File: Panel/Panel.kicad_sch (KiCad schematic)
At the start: 72 parts, among them J1 Conn_01x03, J10 Conn_01x02, J11 Conn_01x03, J12 Conn_01x03, J2 USB_C_Receptacle_USB2.0, J3 Conn_01x02, J4 Conn_02x06_Odd_Even, J5 Conn_01x07, J6 Conn_01x02, J7 Conn_01x02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

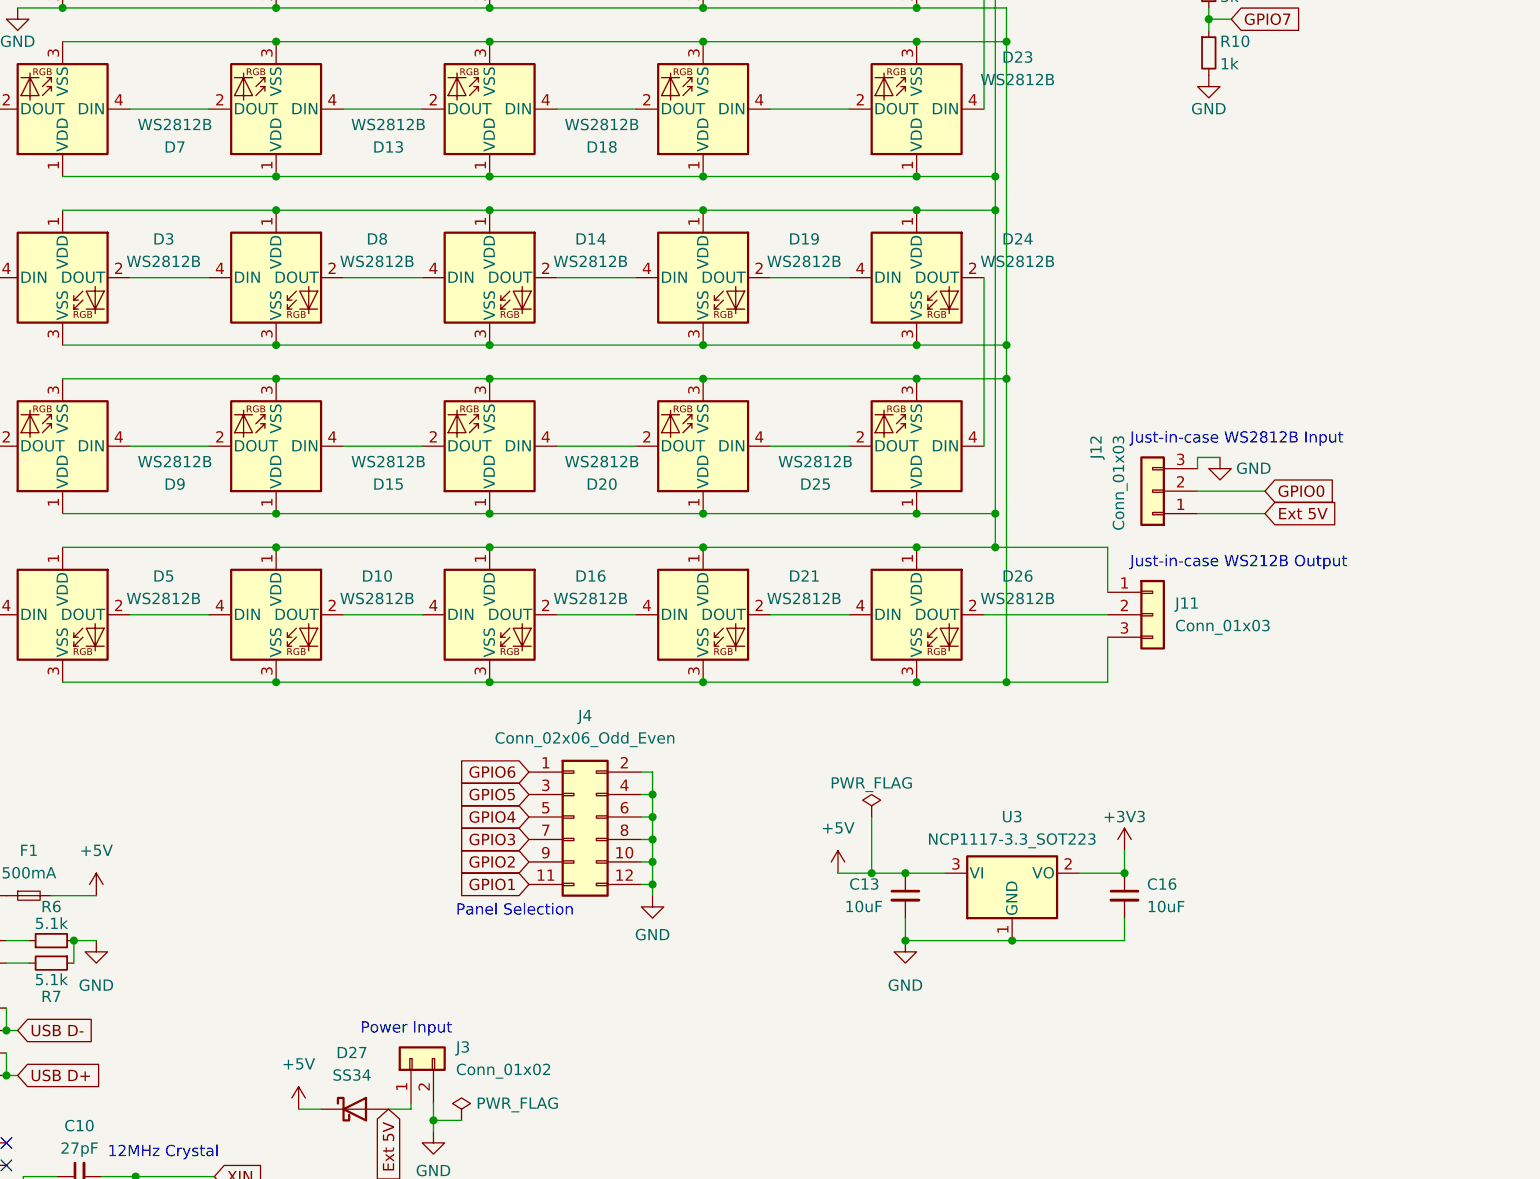
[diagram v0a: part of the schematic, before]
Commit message: Add RS485 functionality & addons, several fixes
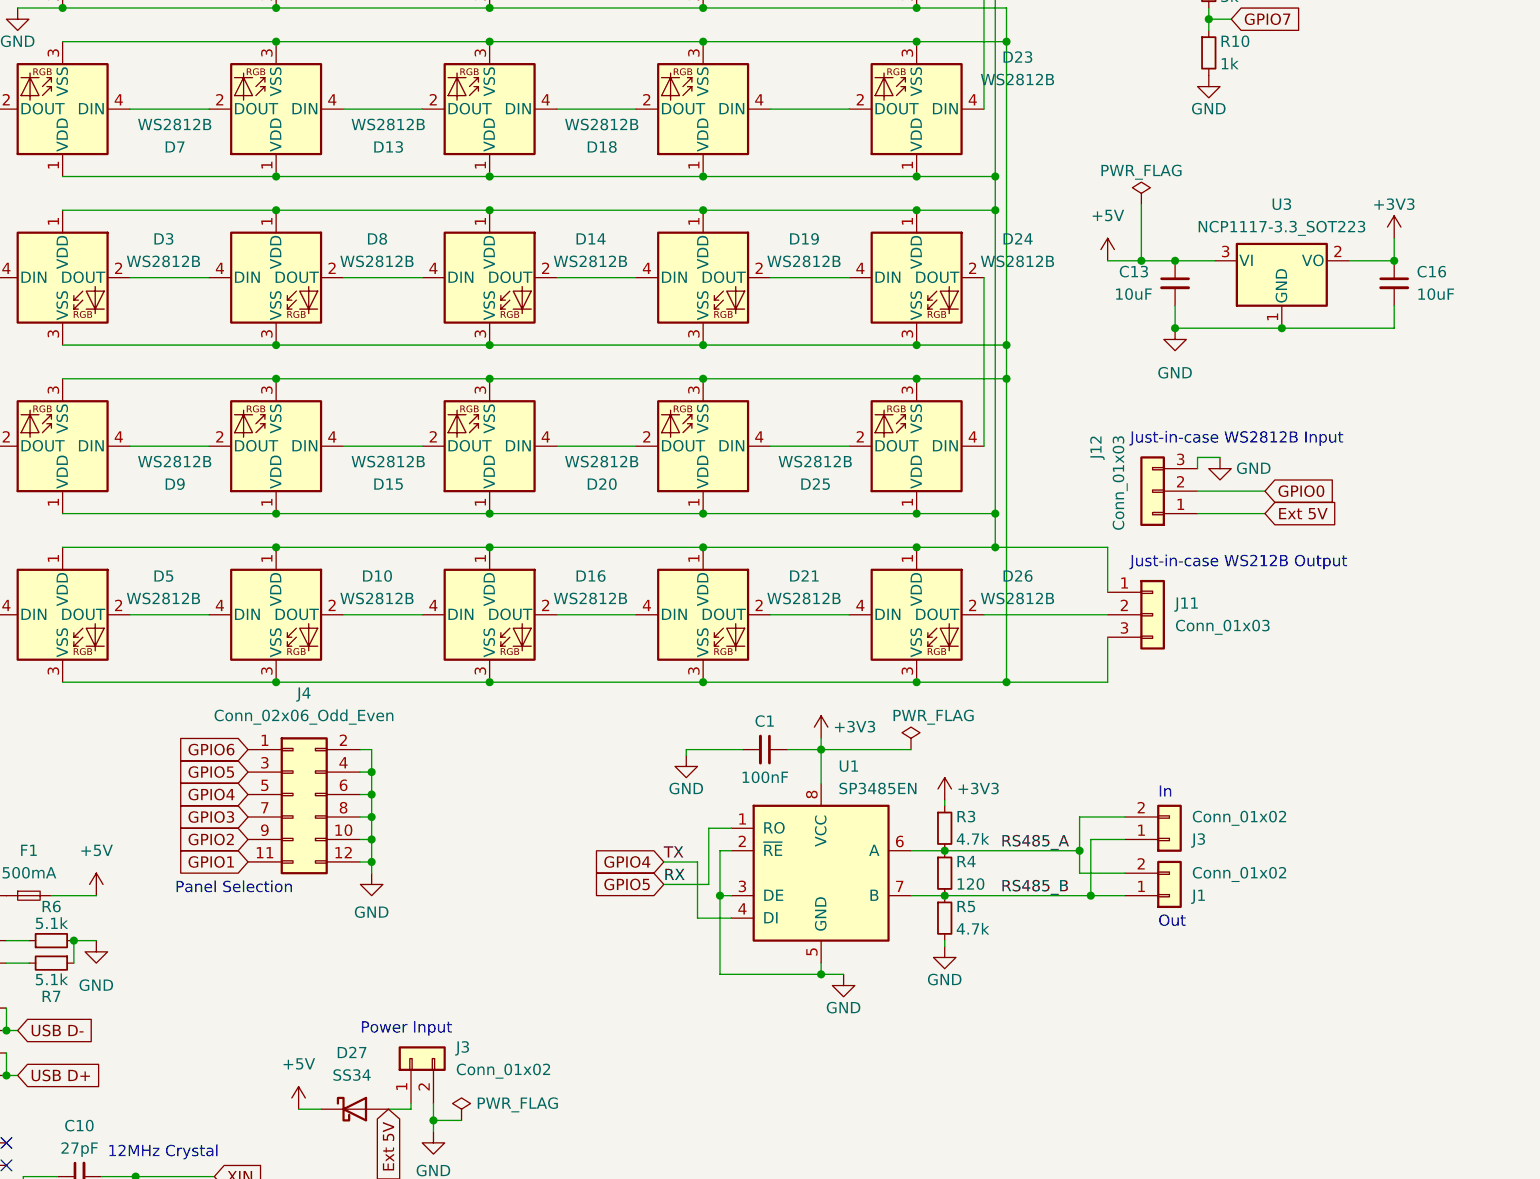
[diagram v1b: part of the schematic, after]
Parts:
- added C1: 100nF, Capacitor_SMD:C_0805_2012Metric_Pad1.18x1.45mm_HandSolder, symbol Device:C_Small
- added J1, J3: Conn_01x02, Connector_JST:JST_XH_S2B-XH-A_1x02_P2.50mm_Horizontal, symbol Connector_Generic:Conn_01x02
- added R3, R5: 4.7k, Resistor_SMD:R_0805_2012Metric_Pad1.20x1.40mm_HandSolder, symbol Device:R_Small
- added R4: 120, Resistor_SMD:R_0805_2012Metric_Pad1.20x1.40mm_HandSolder, symbol Device:R_Small
- added U1: SP3485EN, Package_SO:SOIC-8_3.9x4.9mm_P1.27mm, symbol Interface_UART:SP3485EN
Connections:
- net +3V3: now also C1.1, R3.1, U1.8 (VCC)
- net GND: now also C1.2, R5.2, U1.2 (~{RE}), U1.3 (DE), U1.5 (GND)
- net GPIO4: now also U1.4 (DI)
- net GPIO5: now also U1.1 (RO)
- new net RS485_A: J1.2 (Pin_2), J3.2 (Pin_2), R3.2, R4.1, U1.6 (A)
- new net RS485_B: J1.1 (Pin_1), J3.1 (Pin_1), R4.2, R5.1, U1.7 (B)
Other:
- note added: "In"
- note added: "Out"
- moved on the sheet: C13, C16, J4, U3

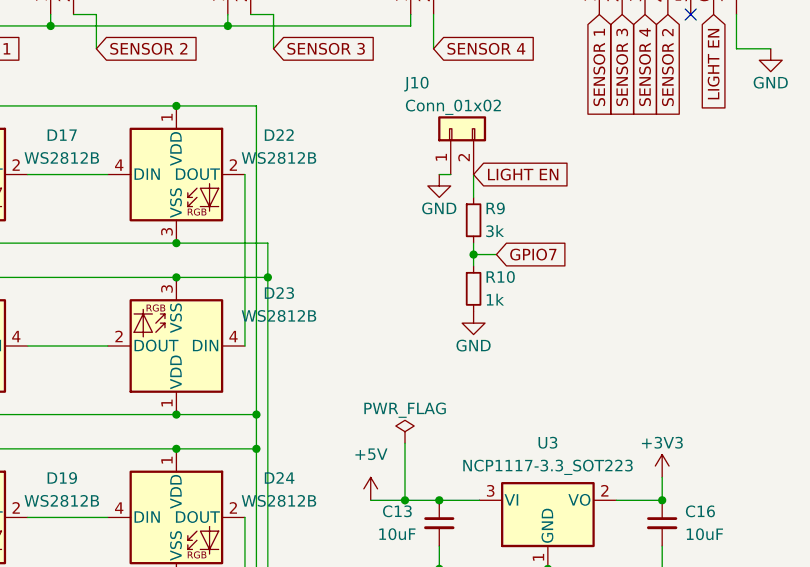
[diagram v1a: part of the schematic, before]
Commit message: Add voltage divider bypass for home pad use
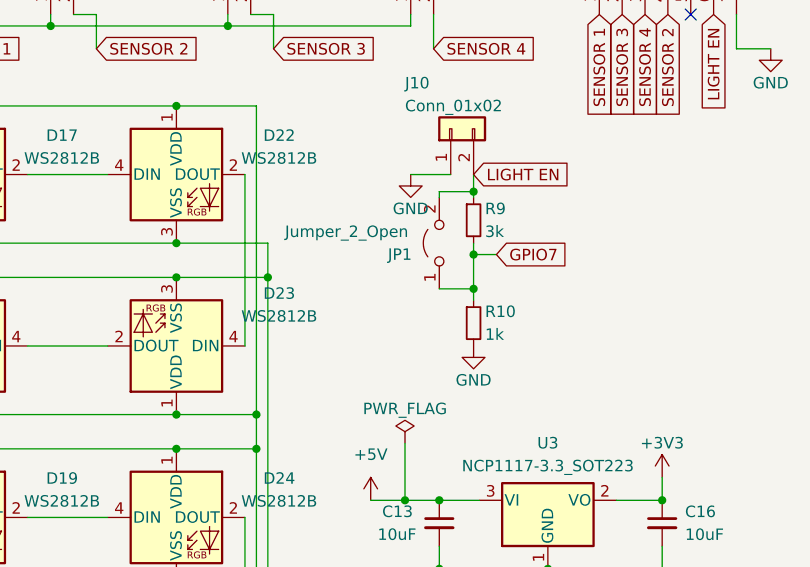
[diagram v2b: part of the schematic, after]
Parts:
- added JP1: Jumper_2_Open, Jumper:SolderJumper-2_P1.3mm_Open_RoundedPad1.0x1.5mm, symbol Jumper:Jumper_2_Open
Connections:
- net GPIO7: now also JP1.1 (A)
- net LIGHT EN: now also JP1.2 (B)
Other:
- moved on the sheet: R10
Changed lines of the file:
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@@
   (junction (at 113.03 171.45) (diameter 0) (color 0 0 0 0)
   )
+  (junction (at 248.92 55.88) (diameter 0) (color 0 0 0 0)
+  )
   (junction (at 191.77 88.9) (diameter 0) (color 0 0 0 0)
   )
   (junction (at 116.205 17.78) (diameter 0) (color 0 0 0 0)
   )
+  (junction (at 248.92 45.085) (diameter 0) (color 0 0 0 0)
+  )
   (junction (at 143.51 88.9) (diameter 0) (color 0 0 0 0)
   )
@@
     (stroke (width 0) (type default))
   )
-  (wire (pts (xy 245.11 43.18) (xy 246.38 43.18))
+  (wire (pts (xy 241.935 43.18) (xy 246.38 43.18))
     (stroke (width 0) (type default))
   )
@@
     (stroke (width 0) (type default))
   )
+  (wire (pts (xy 245.11 45.085) (xy 248.92 45.085))
+    (stroke (width 0) (type default))
+  )
   (wire (pts (xy 201.93 26.67) (xy 201.93 25.4))
     (stroke (width 0) (type default))
@@
     (stroke (width 0) (type default))
   )
+  (wire (pts (xy 248.92 55.88) (xy 248.92 57.15))
+    (stroke (width 0) (type default))
+  )
   (wire (pts (xy 24.765 158.75) (xy 27.305 158.75))
     (stroke (width 0) (type default))
@@
     (stroke (width 0) (type default))
   )
-  (wire (pts (xy 248.92 52.07) (xy 248.92 53.34))
+  (wire (pts (xy 248.92 52.07) (xy 248.92 55.88))
     (stroke (width 0) (type default))
   )
@@
     (stroke (width 0) (type default))
   )
-  (wire (pts (xy 248.92 43.18) (xy 248.92 45.72))
+  (wire (pts (xy 248.92 43.18) (xy 248.92 45.085))
     (stroke (width 0) (type default))
   )
@@
     (stroke (width 0) (type default))
   )
+  (wire (pts (xy 245.11 55.88) (xy 248.92 55.88))
+    (stroke (width 0) (type default))
+  )
   (wire (pts (xy 31.115 178.435) (xy 43.18 178.435))
     (stroke (width 0) (type default))
@@
     (stroke (width 0) (type default))
   )
+  (wire (pts (xy 245.11 45.72) (xy 245.11 45.085))
+    (stroke (width 0) (type default))
+  )
   (wire (pts (xy 95.885 39.37) (xy 95.885 38.1))
     (stroke (width 0) (type default))
@@
     (stroke (width 0) (type default))
   )
+  (wire (pts (xy 248.92 45.085) (xy 248.92 45.72))
+    (stroke (width 0) (type default))
+  )
   (wire (pts (xy 127 81.28) (xy 135.89 81.28))
     (stroke (width 0) (type default))
@@
     )
   )
-  (symbol (lib_id "power:GND") (at 245.11 43.18 0) (unit 1)
+  (symbol (lib_id "power:GND") (at 241.935 43.18 0) (unit 1)
     (in_bom yes) (on_board yes) (dnp no)
-    (property "Reference" "#PWR0106" (at 245.11 49.53 0)
+    (property "Reference" "#PWR0106" (at 241.935 49.53 0)
       (effects (font (size 1.27 1.27)) hide)
     )
-    (property "Value" "GND" (at 245.11 46.99 0)
+    (property "Value" "GND" (at 241.935 46.99 0)
       (effects (font (size 1.27 1.27)))
     )
-    (property "Footprint" "" (at 245.11 43.18 0)
+    (property "Footprint" "" (at 241.935 43.18 0)
       (effects (font (size 1.27 1.27)) hide)
     )
-    (property "Datasheet" "" (at 245.11 43.18 0)
+    (property "Datasheet" "" (at 241.935 43.18 0)
       (effects (font (size 1.27 1.27)) hide)
     )
@@
     )
   )
-  (symbol (lib_id "Device:R_Small") (at 248.92 55.88 0) (unit 1)
+  (symbol (lib_id "Device:R_Small") (at 248.92 59.69 0) (unit 1)
     (in_bom yes) (on_board yes) (dnp no)
-    (property "Reference" "R10" (at 250.19 54.61 0)
+    (property "Reference" "R10" (at 250.19 58.42 0)
       (effects (font (size 1.27 1.27)) (justify left))
     )
-    (property "Value" "1k" (at 250.19 57.15 0)
+    (property "Value" "1k" (at 250.19 60.96 0)
       (effects (font (size 1.27 1.27)) (justify left))
     )
-    (property "Footprint" "Resistor_SMD:R_0402_1005Metric_Pad0.72x0.64mm_HandSolder" (at 248.92 55.88 0)
+    (property "Footprint" "Resistor_SMD:R_0402_1005Metric_Pad0.72x0.64mm_HandSolder" (at 248.92 59.69 0)
       (effects (font (size 1.27 1.27)) hide)
     )
-    (property "Datasheet" "~" (at 248.92 55.88 0)
+    (property "Datasheet" "~" (at 248.92 59.69 0)
       (effects (font (size 1.27 1.27)) hide)
     )
-    (property "LCSC" "C106235" (at 248.92 55.88 0)
+    (property "LCSC" "C106235" (at 248.92 59.69 0)
       (effects (font (size 1.27 1.27)) hide)
     )
@@
     )
   )
+  (symbol (lib_id "Jumper:Jumper_2_Open") (at 245.11 50.8 90) (unit 1)
+    (in_bom yes) (on_board yes) (dnp no)
+    (property "Reference" "JP1" (at 239.395 52.07 90)
+      (effects (font (size 1.27 1.27)) (justify right))
+    )
+    (property "Value" "Jumper_2_Open" (at 227.965 49.53 90)
+      (effects (font (size 1.27 1.27)) (justify right))
+    )
+    (property "Footprint" "Jumper:SolderJumper-2_P1.3mm_Open_RoundedPad1.0x1.5mm" (at 245.11 50.8 0)
+      (effects (font (size 1.27 1.27)) hide)
+    )
+    (property "Datasheet" "~" (at 245.11 50.8 0)
+      (effects (font (size 1.27 1.27)) hide)
+    )
+    (pin "1")
+    (pin "2")
+    (instances
+      (project "Panel"
+        (path "/f55927e3-6490-4e79-9229-dceeb24f0064"
+          (reference "JP1") (unit 1)
+        )
+      )
+    )
+  )
   (symbol (lib_id "power:GND") (at 40.005 154.305 0) (unit 1)
     (in_bom yes) (on_board yes) (dnp no)
@@
     )
   )
-  (symbol (lib_id "power:GND") (at 248.92 58.42 0) (unit 1)
+  (symbol (lib_id "power:GND") (at 248.92 62.23 0) (unit 1)
     (in_bom yes) (on_board yes) (dnp no)
-    (property "Reference" "#PWR0105" (at 248.92 64.77 0)
+    (property "Reference" "#PWR0105" (at 248.92 68.58 0)
       (effects (font (size 1.27 1.27)) hide)
     )
-    (property "Value" "GND" (at 248.92 62.23 0)
+    (property "Value" "GND" (at 248.92 66.04 0)
       (effects (font (size 1.27 1.27)))
     )
-    (property "Footprint" "" (at 248.92 58.42 0)
+    (property "Footprint" "" (at 248.92 62.23 0)
       (effects (font (size 1.27 1.27)) hide)
     )
-    (property "Datasheet" "" (at 248.92 58.42 0)
+    (property "Datasheet" "" (at 248.92 62.23 0)
       (effects (font (size 1.27 1.27)) hide)
     )

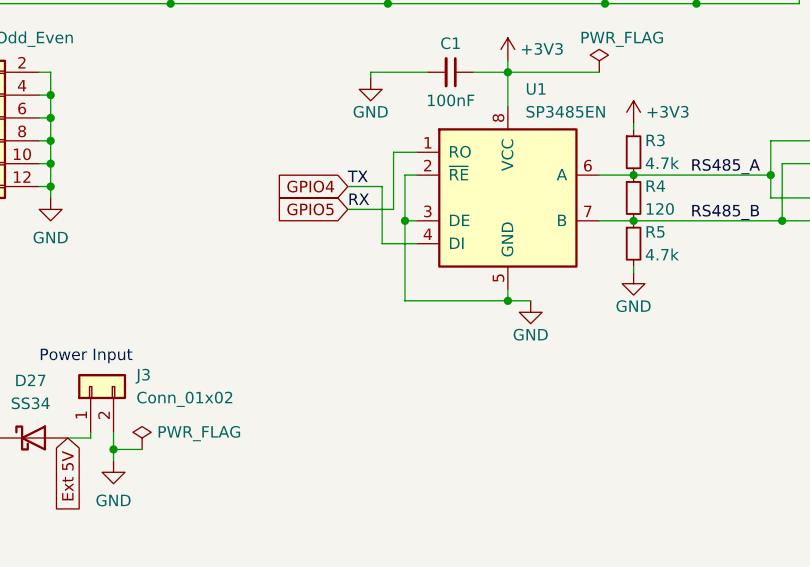
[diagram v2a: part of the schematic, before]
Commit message: Fix an oopsie, control RE/DE via GPIO by default
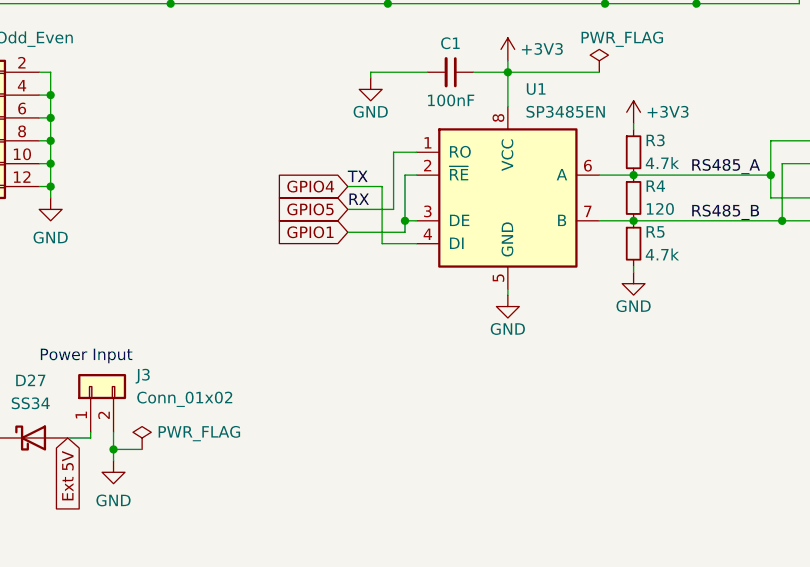
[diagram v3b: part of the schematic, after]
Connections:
- net GND: no longer U1.2 (~{RE}), U1.3 (DE)
- net GPIO1: now also U1.2 (~{RE}), U1.3 (DE)
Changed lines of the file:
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@@
   (junction (at 143.51 88.9) (diameter 0) (color 0 0 0 0)
   )
-  (junction (at 205.105 160.02) (diameter 0) (color 0 0 0 0)
-  )
   (junction (at 143.51 73.66) (diameter 0) (color 0 0 0 0)
   )
@@
   (junction (at 215.9 92.71) (diameter 0) (color 0 0 0 0)
   )
-  (junction (at 193.675 151.13) (diameter 0) (color 0 0 0 0)
-  )
   (junction (at 115.57 35.56) (diameter 0) (color 0 0 0 0)
   )
@@
   (junction (at 143.51 107.95) (diameter 0) (color 0 0 0 0)
   )
+  (junction (at 193.675 151.13) (diameter 0) (color 0 0 0 0)
+  )
   (junction (at 127.635 182.88) (diameter 0) (color 0 0 0 0)
   )
@@
     (stroke (width 0) (type default))
   )
-  (wire (pts (xy 193.675 151.13) (xy 193.675 160.02))
-    (stroke (width 0) (type default))
-  )
   (wire (pts (xy 235.585 151.13) (xy 235.585 144.78))
     (stroke (width 0) (type default))
@@
     (stroke (width 0) (type default))
   )
+  (wire (pts (xy 193.675 152.4) (xy 187.325 152.4))
+    (stroke (width 0) (type default))
+  )
   (wire (pts (xy 226.06 127) (xy 237.49 127))
     (stroke (width 0) (type default))
@@
     (stroke (width 0) (type default))
   )
+  (wire (pts (xy 193.675 151.13) (xy 193.675 152.4))
+    (stroke (width 0) (type default))
+  )
   (wire (pts (xy 192.405 143.51) (xy 194.945 143.51))
     (stroke (width 0) (type default))
@@
     (stroke (width 0) (type default))
   )
-  (wire (pts (xy 207.645 160.02) (xy 205.105 160.02))
-    (stroke (width 0) (type default))
-  )
   (wire (pts (xy 187.325 149.86) (xy 192.405 149.86))
     (stroke (width 0) (type default))
@@
     (stroke (width 0) (type default))
   )
-  (wire (pts (xy 205.105 158.75) (xy 205.105 160.02))
+  (wire (pts (xy 205.105 158.75) (xy 205.105 159.385))
     (stroke (width 0) (type default))
   )
@@
     (stroke (width 0) (type default))
   )
-  (wire (pts (xy 193.675 160.02) (xy 205.105 160.02))
-    (stroke (width 0) (type default))
-  )
   (wire (pts (xy 153.035 144.78) (xy 154.305 144.78))
     (stroke (width 0) (type default))
@@
     )
   )
+  (global_label "GPIO1" (shape input) (at 187.325 152.4 180) (fields_autoplaced)
+    (effects (font (size 1.27 1.27)) (justify right))
+    (property "Intersheetrefs" "${INTERSHEET_REFS}" (at 178.7344 152.4 0)
+      (effects (font (size 1.27 1.27)) (justify right) hide)
+    )
+  )
   (global_label "SENSOR 1" (shape input) (at 187.325 29.21 0) (fields_autoplaced)
     (effects (font (size 1.27 1.27)) (justify left))
@@
     )
   )
-  (symbol (lib_id "power:GND") (at 207.645 160.02 0) (unit 1)
+  (symbol (lib_id "power:GND") (at 205.105 159.385 0) (unit 1)
     (in_bom yes) (on_board yes) (dnp no)
-    (property "Reference" "#PWR03" (at 207.645 166.37 0)
+    (property "Reference" "#PWR03" (at 205.105 165.735 0)
       (effects (font (size 1.27 1.27)) hide)
     )
-    (property "Value" "GND" (at 207.645 163.83 0)
+    (property "Value" "GND" (at 205.105 163.195 0)
       (effects (font (size 1.27 1.27)))
     )
-    (property "Footprint" "" (at 207.645 160.02 0)
+    (property "Footprint" "" (at 205.105 159.385 0)
       (effects (font (size 1.27 1.27)) hide)
     )
-    (property "Datasheet" "" (at 207.645 160.02 0)
+    (property "Datasheet" "" (at 205.105 159.385 0)
       (effects (font (size 1.27 1.27)) hide)
     )

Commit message: Replaced USB C port with cheaper alternative
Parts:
- J2: footprint Connector_USB:USB_C_Receptacle_GCT_USB4085 -> Connector_USB:USB_C_Receptacle_G-Switch_GT-USB-7010ASV
